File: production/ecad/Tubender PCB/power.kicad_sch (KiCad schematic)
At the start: 62 parts, among them Q1 CSD19502Q5B, Q2 CSD19534Q5A, U1 LMR36520FADDAR, U11 LM5146RGYR, U13 LM5017SDX/NOPB, U5 TPSM265R1V5SILR

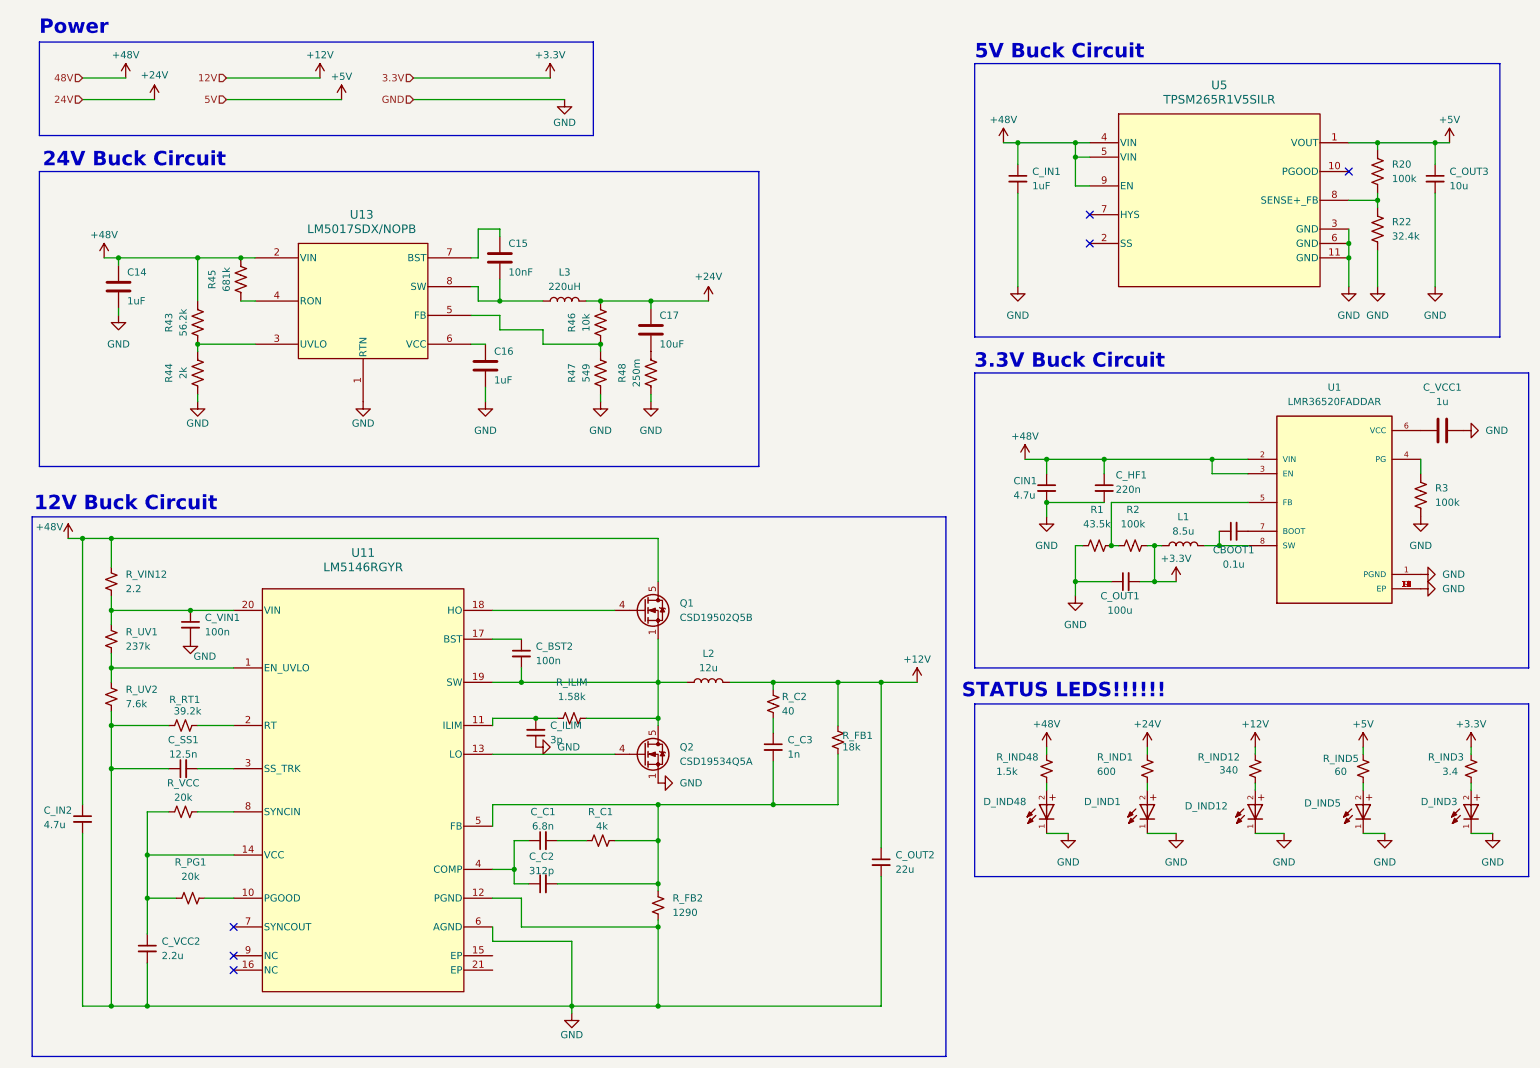
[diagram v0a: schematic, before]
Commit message: Adding Test Points
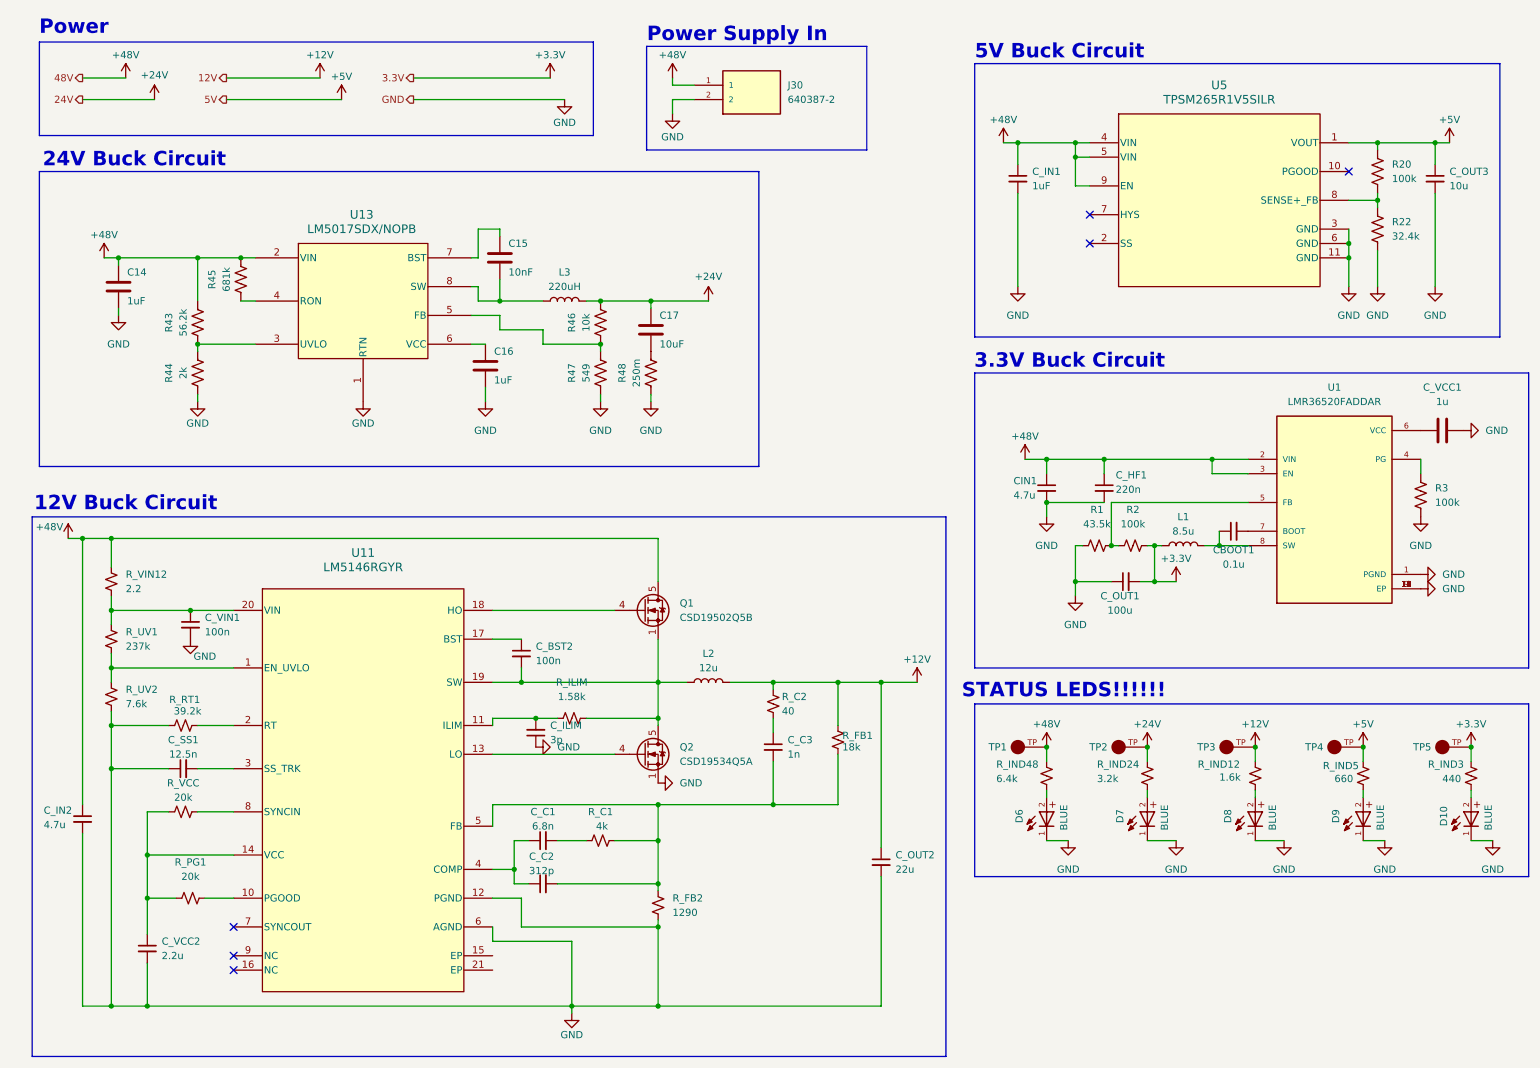
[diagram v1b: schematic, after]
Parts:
- removed D_IND1, D_IND12, D_IND3, D_IND48, D_IND5: WL-SMCW_0603, WL-SMCW_0603:WL-SMCW_0603, symbol WL-SMCW_0603:WL-SMCW_0603
- added D10, D6, D7, D8, D9: BLUE, WL-SMCW_0603:WL-SMCW_0603, symbol WL-SMCW_0603:WL-SMCW_0603
- added J30: 640387-2, 640387-2:TE_640387-2, symbol 640387-2:640387-2
- added TP1, TP2, TP3, TP4, TP5: 5006, 5006:KEYSTONE_5006, symbol 5006:5006
- R_IND12: value 340 -> 1.6k
- R_IND24: renamed from R_IND1; value 600 -> 3.2k
- R_IND3: value 3.4 -> 440
- R_IND48: value 1.5k -> 6.4k
- R_IND5: value 60 -> 660
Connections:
- net +12V: now also TP3.TP
- net +24V: now also TP2.TP
- net +3.3V: now also TP5.TP
- net +48V: now also J30.1, TP1.TP
- net +5V: now also TP4.TP
- net GND: now also D10.1, D6.1, D7.1, D8.1, D9.1, J30.2
- net at R_IND12.2: now also D8.2
- net at R_IND3.2: now also D10.2
- net at R_IND24.2: now also D7.2
- net at R_IND5.2: now also D9.2
- net at R_IND48.2: now also D6.2
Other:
- note added: "Power Supply In"
- moved on the sheet: R_IND12, R_IND24, R_IND3, R_IND48, R_IND5

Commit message: annotate schematic
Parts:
- renumbered CBOOT1 to CBOOT33, C15 to C_BST2, C_BST2 to C_BST3, C_HF1 to C_HF33, C_ILIM to C_ILIM1, CIN1 to C_IN33, C_IN1 to C_IN5, C_OUT2 to C_OUT12, C17 to C_OUT2, C_OUT1 to C_OUT33, C16 to C_VCC3, C_VCC1 to C_VCC33, C14 to C_VIN2, L3 to L_SW2, Q1 to Q_HI1, Q2 to Q_LO1, R_ILIM to R_ILIM1, R45 to R_ON1, R48 to R_OUT2, R43 to R_UV3, R44 to R_UV4, R_VCC to R_VCC1, U11 to U12
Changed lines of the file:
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@@
 		(on_board yes)
 		(dnp no)
-		(property "Reference" "C16"
+		(property "Reference" "C_VCC3"
 			(at 95.504 72.39 0)
 			(effects
@@
 			(project "Tubender PCB"
 				(path "/3e1aedd0-6089-4edb-92c7-0c31da2e7927/3bac66d4-e1f2-42c2-b72f-be753c44ff12"
-					(reference "C16")
+					(reference "C_VCC3")
 					(unit 1)
 				)
@@
 		(dnp no)
 		(fields_autoplaced yes)
-		(property "Reference" "Q1"
+		(property "Reference" "Q_HI1"
 			(at 128.27 116.8399 0)
 			(effects
@@
 			(project "Tubender PCB"
 				(path "/3e1aedd0-6089-4edb-92c7-0c31da2e7927/3bac66d4-e1f2-42c2-b72f-be753c44ff12"
-					(reference "Q1")
+					(reference "Q_HI1")
 					(unit 1)
 				)
@@
 		(dnp no)
 		(fields_autoplaced yes)
-		(property "Reference" "U11"
-			(at 72.39 107.95 0)
+		(property "Reference" "U12"
+			(at 72.39 109.22 0)
 			(effects
 				(font
@@
 		)
 		(property "Value" "LM5146RGYR"
-			(at 72.39 110.49 0)
+			(at 72.39 111.76 0)
 			(effects
 				(font
@@
 			(project ""
 				(path "/3e1aedd0-6089-4edb-92c7-0c31da2e7927/3bac66d4-e1f2-42c2-b72f-be753c44ff12"
-					(reference "U11")
+					(reference "U12")
 					(unit 1)
 				)
@@
 		(dnp no)
 		(fields_autoplaced yes)
-		(property "Reference" "Q2"
+		(property "Reference" "Q_LO1"
 			(at 128.27 142.2399 0)
 			(effects
@@
 			(project ""
 				(path "/3e1aedd0-6089-4edb-92c7-0c31da2e7927/3bac66d4-e1f2-42c2-b72f-be753c44ff12"
-					(reference "Q2")
+					(reference "Q_LO1")
 					(unit 1)
 				)
@@
 		(on_board yes)
 		(dnp no)
-		(property "Reference" "C_HF1"
+		(property "Reference" "C_HF33"
 			(at 205.232 94.234 0)
 			(effects
@@
 			(project "Tubender PCB"
 				(path "/3e1aedd0-6089-4edb-92c7-0c31da2e7927/3bac66d4-e1f2-42c2-b72f-be753c44ff12"
-					(reference "C_HF1")
+					(reference "C_HF33")
 					(unit 1)
 				)
@@
 		(dnp no)
 		(fields_autoplaced yes)
-		(property "Reference" "C_ILIM"
+		(property "Reference" "C_ILIM1"
 			(at 105.41 138.4235 0)
 			(effects
@@
 			(project ""
 				(path "/3e1aedd0-6089-4edb-92c7-0c31da2e7927/3bac66d4-e1f2-42c2-b72f-be753c44ff12"
-					(reference "C_ILIM")
+					(reference "C_ILIM1")
 					(unit 1)
 				)
@@
 		(on_board yes)
 		(dnp no)
-		(property "Reference" "C17"
+		(property "Reference" "C_OUT2"
 			(at 124.714 66.04 0)
 			(effects
@@
 			(project "Tubender PCB"
 				(path "/3e1aedd0-6089-4edb-92c7-0c31da2e7927/3bac66d4-e1f2-42c2-b72f-be753c44ff12"
-					(reference "C17")
+					(reference "C_OUT2")
 					(unit 1)
 				)
@@
 		(dnp no)
 		(fields_autoplaced yes)
-		(property "Reference" "C_VCC1"
+		(property "Reference" "C_VCC33"
 			(at 262.89 78.74 90)
 			(effects
@@
 			(project "Tubender PCB"
 				(path "/3e1aedd0-6089-4edb-92c7-0c31da2e7927/3bac66d4-e1f2-42c2-b72f-be753c44ff12"
-					(reference "C_VCC1")
+					(reference "C_VCC33")
 					(unit 1)
 				)
@@
 		(dnp no)
 		(fields_autoplaced yes)
-		(property "Reference" "C_OUT2"
+		(property "Reference" "C_OUT12"
 			(at 166.37 161.2962 0)
 			(effects
@@
 			(project ""
 				(path "/3e1aedd0-6089-4edb-92c7-0c31da2e7927/3bac66d4-e1f2-42c2-b72f-be753c44ff12"
-					(reference "C_OUT2")
+					(reference "C_OUT12")
 					(unit 1)
 				)
@@
 		(dnp no)
 		(fields_autoplaced yes)
-		(property "Reference" "C_IN1"
+		(property "Reference" "C_IN5"
 			(at 190.5 40.6462 0)
 			(effects
@@
 			(project "Tubender Main_PCB"
 				(path "/3e1aedd0-6089-4edb-92c7-0c31da2e7927/3bac66d4-e1f2-42c2-b72f-be753c44ff12"
-					(reference "C_IN1")
+					(reference "C_IN5")
 					(unit 1)
 				)
@@
 		(on_board yes)
 		(dnp no)
-		(property "Reference" "CIN1"
+		(property "Reference" "C_IN33"
 			(at 187.198 95.25 0)
 			(effects
@@
 			(project "Tubender PCB"
 				(path "/3e1aedd0-6089-4edb-92c7-0c31da2e7927/3bac66d4-e1f2-42c2-b72f-be753c44ff12"
-					(reference "CIN1")
+					(reference "C_IN33")
 					(unit 1)
 				)
@@
 		(dnp no)
 		(fields_autoplaced yes)
-		(property "Reference" "L3"
+		(property "Reference" "L_SW2"
 			(at 107.95 58.42 90)
 			(effects
@@
 			(project "Tubender PCB"
 				(path "/3e1aedd0-6089-4edb-92c7-0c31da2e7927/3bac66d4-e1f2-42c2-b72f-be753c44ff12"
-					(reference "L3")
+					(reference "L_SW2")
 					(unit 1)
 				)
@@
 		(dnp no)
 		(fields_autoplaced yes)
-		(property "Reference" "C_BST2"
+		(property "Reference" "C_BST3"
 			(at 102.87 124.4662 0)
 			(effects
@@
 			(project ""
 				(path "/3e1aedd0-6089-4edb-92c7-0c31da2e7927/3bac66d4-e1f2-42c2-b72f-be753c44ff12"
-					(reference "C_BST2")
+					(reference "C_BST3")
 					(unit 1)
 				)
@@
 		(on_board yes)
 		(dnp no)
-		(property "Reference" "C14"
+		(property "Reference" "C_VIN2"
 			(at 30.734 58.42 0)
 			(effects
@@
 			(project "Tubender PCB"
 				(path "/3e1aedd0-6089-4edb-92c7-0c31da2e7927/3bac66d4-e1f2-42c2-b72f-be753c44ff12"
-					(reference "C14")
+					(reference "C_VIN2")
 					(unit 1)
 				)
@@
 		(on_board yes)
 		(dnp no)
-		(property "Reference" "R_VCC"
+		(property "Reference" "R_VCC1"
 			(at 40.64 148.59 90)
 			(effects
@@
 			(project ""
 				(path "/3e1aedd0-6089-4edb-92c7-0c31da2e7927/3bac66d4-e1f2-42c2-b72f-be753c44ff12"
-					(reference "R_VCC")
+					(reference "R_VCC1")
 					(unit 1)
 				)
@@
 		(dnp no)
 		(fields_autoplaced yes)
-		(property "Reference" "R_ILIM"
+		(property "Reference" "R_ILIM1"
 			(at 109.22 130.81 90)
 			(effects
@@
 			(project ""
 				(path "/3e1aedd0-6089-4edb-92c7-0c31da2e7927/3bac66d4-e1f2-42c2-b72f-be753c44ff12"
-					(reference "R_ILIM")
+					(reference "R_ILIM1")
 					(unit 1)
 				)
@@
 		(on_board yes)
 		(dnp no)
-		(property "Reference" "C15"
+		(property "Reference" "C_BST2"
 			(at 98.044 53.34 0)
 			(effects
@@
 			(project "Tubender PCB"
 				(path "/3e1aedd0-6089-4edb-92c7-0c31da2e7927/3bac66d4-e1f2-42c2-b72f-be753c44ff12"
-					(reference "C15")
+					(reference "C_BST2")
 					(unit 1)
 				)
@@
 		(on_board yes)
 		(dnp no)
-		(property "Reference" "R45"
+		(property "Reference" "R_ON1"
 			(at 45.72 59.69 90)
 			(effects
@@
 			(project "Tubender PCB"
 				(path "/3e1aedd0-6089-4edb-92c7-0c31da2e7927/3bac66d4-e1f2-42c2-b72f-be753c44ff12"
-					(reference "R45")
+					(reference "R_ON1")
 					(unit 1)
 				)
@@
 		(on_board yes)
 		(dnp no)
-		(property "Reference" "R44"
+		(property "Reference" "R_UV4"
 			(at 38.1 76.2 90)
 			(effects
@@
 			(project "Tubender PCB"
 				(path "/3e1aedd0-6089-4edb-92c7-0c31da2e7927/3bac66d4-e1f2-42c2-b72f-be753c44ff12"
-					(reference "R44")
+					(reference "R_UV4")
 					(unit 1)
 				)
@@
 		(on_board yes)
 		(dnp no)
-		(property "Reference" "R48"
+		(property "Reference" "R_OUT2"
 			(at 118.11 76.2 90)
 			(effects
@@
 			(project "Tubender PCB"
 				(path "/3e1aedd0-6089-4edb-92c7-0c31da2e7927/3bac66d4-e1f2-42c2-b72f-be753c44ff12"
-					(reference "R48")
+					(reference "R_OUT2")
 					(unit 1)
 				)
@@
 		(on_board yes)
 		(dnp no)
-		(property "Reference" "CBOOT1"
+		(property "Reference" "CBOOT33"
 			(at 226.06 107.442 90)
 			(effects
@@
 			(project "Tubender PCB"
 				(path "/3e1aedd0-6089-4edb-92c7-0c31da2e7927/3bac66d4-e1f2-42c2-b72f-be753c44ff12"
-					(reference "CBOOT1")
+					(reference "CBOOT33")
 					(unit 1)
 				)
@@
 		(on_board yes)
 		(dnp no)
-		(property "Reference" "C_OUT1"
+		(property "Reference" "C_OUT33"
 			(at 205.994 115.57 90)
 			(effects
@@
 			(project ""
 				(path "/3e1aedd0-6089-4edb-92c7-0c31da2e7927/3bac66d4-e1f2-42c2-b72f-be753c44ff12"
-					(reference "C_OUT1")
+					(reference "C_OUT33")
 					(unit 1)
 				)
@@
 		(on_board yes)
 		(dnp no)
-		(property "Reference" "R43"
+		(property "Reference" "R_UV3"
 			(at 38.1 67.31 90)
 			(effects
@@
 			(project "Tubender PCB"
 				(path "/3e1aedd0-6089-4edb-92c7-0c31da2e7927/3bac66d4-e1f2-42c2-b72f-be753c44ff12"
-					(reference "R43")
+					(reference "R_UV3")
 					(unit 1)
 				)
